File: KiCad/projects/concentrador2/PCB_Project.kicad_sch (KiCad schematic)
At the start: 43 parts, among them J1 54602-908LF, P1 Grabador, P2 Entrada fuente externa, P4 Header 20X2, P5 Header 2, U1 DSPIC33EP256MC202-I/SP, U2 STEP_DOWN_CONVERTER, U3 LD33V, U4 MAX485, U5 DS3234S#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

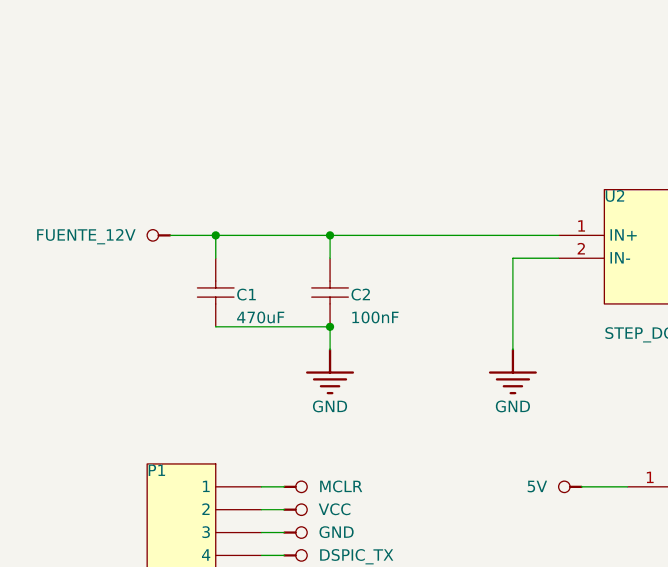
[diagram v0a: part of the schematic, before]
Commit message: Migracion a SMD
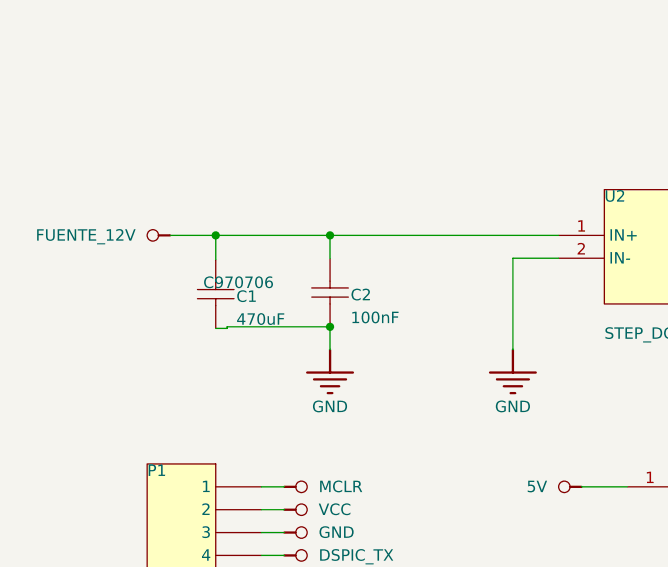
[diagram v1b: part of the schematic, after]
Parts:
- C1: LCSC (none) -> C970706
- R1: footprint F__UDecimo_practicasLaborales2_proyectos_archivosAltium_completos_int3_R-007 ACELEROGRAFO ADXL355 CONCENTRADOR V1_PCB_P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 -> Resistor_SMD:R_0603_1608Metric
- R13, R14, R15, R16, R17, R18, R3, R4: footprint AXIAL-0.3 -> Resistor_SMD:R_0603_1608Metric
- R2, R5: footprint AXIAL-0.3 RES-1/4W -> Resistor_SMD:R_0603_1608Metric
- U3: footprint SOT-223 -> Package_TO_SOT_SMD:SOT-223

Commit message: Fase 3
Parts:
- C10: LCSC (none) -> C3845218
- C12, C13, C15, C2, C4, C5, C7: LCSC (none) -> C141382
- C3: LCSC (none) -> C970695
- C6: LCSC (none) -> C53084506
- Ce: renamed from C8; LCSC (none) -> C141382
- Ce: renamed from C9; LCSC (none) -> C53084506
- R1, R16, R18: LCSC (none) -> C17902
- R13, R14, R2, R5: LCSC (none) -> C22978
- R15, R17: LCSC (none) -> C17903
- R3: LCSC (none) -> C17900
- R4: LCSC (none) -> C17935
- S1: LCSC (none) -> C231329
- U3: LCSC (none) -> C35879
- U4, U9: LCSC (none) -> C481667

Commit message: Fase 4 - Asignación para PCBA
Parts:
- removed BT1: Bateria, Bateria-DS1307, symbol LibreriaRSA:root_0_BateriaDS1307_LibreriaRSA.IntLib
- removed D1: 1N914, DO-35, symbol Miscellaneous Devices:root_0_Diode 1N914_Miscellaneous Devices.IntLib
- added BT2: Battery, Battery:BatteryHolder_Keystone_500, symbol Device:Battery
- added D1: 1N914, Diode_THT:D_DO-35_SOD27_P7.62mm_Horizontal, symbol Diode:1N914
- C1: footprint C100UFB -> Capacitor_SMD:C_Elec_8x10.2; LCSC C970706 -> C2858857
- C10: footprint RAD0.2 -> Capacitor_SMD:C_0402_1005Metric; LCSC C3845218 -> C29266
- C12, C13, C15, C2, C4, C5, C6, C7: footprint RAD0.2 -> Capacitor_SMD:C_0402_1005Metric
- C3: footprint C100UFB -> Capacitor_SMD:C_Elec_6.3x7.7
- C8, C9: renamed from Ce; footprint RAD0.2 -> Capacitor_SMD:C_0402_1005Metric
- D2, D4, D5: footprint F__UDecimo_practicasLaborales2_proyectos_archivosAltium_completos_int3_R-007 ACELEROGRAFO ADXL355 CONCENTRADOR V1_PCB_P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 -> LED_SMD:LED_0603_1608Metric
- GPS1: footprint GPS_BREAKOUT_V3 -> (none)
- J1: footprint *AMPHENOL_54602-908LF -> Connector_RJ:RJ45_Amphenol_54602-x08_Horizontal
- P1: footprint HDR1X6 -> Connector_PinHeader_2.54mm:PinHeader_1x06_P2.54mm_Vertical
- P2: footprint MOLEX-2 -> Connector_JST:JST_XH_B2B-XH-A_1x02_P2.50mm_Vertical
- P4: footprint C__Users_Public_Documents_Altium_AD16_Library_Miscellaneous Connectors_Miscellaneous Connectors_3D.PcbLib:HDR2X20 -> Connector_PinHeader_2.54mm:PinHeader_2x20_P2.54mm_Vertical
- P5: footprint Header 1X2 -> Connector_PinHeader_2.54mm:PinHeader_1x02_P2.54mm_Vertical
- R1, R16, R18: footprint Resistor_SMD:R_0603_1608Metric -> Resistor_SMD:R_1206_3216Metric; LCSC C17902 -> C1469
- R13: value Res1 -> 3K3; footprint Resistor_SMD:R_0603_1608Metric -> Resistor_SMD:R_1206_3216Metric; LCSC C22978 -> C26032
- R14, R2, R5: footprint Resistor_SMD:R_0603_1608Metric -> Resistor_SMD:R_1206_3216Metric; LCSC C22978 -> C26032
- R15: value Res1 -> 10k; footprint Resistor_SMD:R_0603_1608Metric -> Resistor_SMD:R_1206_3216Metric; symbol Miscellaneous Devices:root_1_Res1_Miscellaneous Devices.IntLib -> Device:R_US; LCSC C17903 -> C1489
- R17: footprint Resistor_SMD:R_0603_1608Metric -> Resistor_SMD:R_1206_3216Metric; LCSC C17903 -> C1489
- R3: footprint Resistor_SMD:R_0603_1608Metric -> Resistor_SMD:R_1206_3216Metric; LCSC C17900 -> C17936
- R4: footprint Resistor_SMD:R_0603_1608Metric -> Resistor_SMD:R_1206_3216Metric; LCSC C17935 -> C17900
- S1: footprint PULSA4 -> Button_Switch_SMD:SW_SPST_B3U-1000P
- U1: footprint MCHP-SPDIP-SP28 -> Package_DIP:DIP-28_W7.62mm_LongPads
- U2: footprint STEP_DOWN_CONVERTER -> (none)
- U3: footprint Package_TO_SOT_SMD:SOT-223 -> Package_TO_SOT_SMD:SOT-223-3_TabPin2; symbol LibreriaRSA:root_0_LD33V_LibreriaRSA.IntLib -> Regulator_Linear:LD1117S33TR_SOT223
- U4, U9: footprint DIP794W47P254L991H457Q8 -> Package_SO:SOIC-8_3.9x4.9mm_P1.27mm
- U5: footprint 21-0042B_20 -> Package_SO:SOIC-20W_7.5x12.8mm_P1.27mm
- W1: footprint SIP-2 -> Connector_PinHeader_2.54mm:PinHeader_1x02_P2.54mm_Vertical
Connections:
- net 5V: now also U3.3 (VI); no longer U3.1 (IN)
- net GND: now also U3.1 (GND), BT2.2 (-); no longer U3.2 (GND)
- net VCC: now also U3.2 (VO), D1.2 (A); no longer U3.3 (OUT)
- net at R3.2: now also D1.1 (K)
- net NetBT1_0: now reaches U5.16 (VBAT)
- net NetBT1_0: now also BT2.1 (+)
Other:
- moved on the sheet: U3

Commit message: Fase 4 - 2
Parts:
- C1: value Cap -> 470uF; PACKAGE (none) -> SMD,D8xL10.2mm
- C10: PACKAGE (none) -> 0402
- C12, C13, C15: LCSC C141382 -> C1525; PACKAGE (none) -> 0402
- C2, C4, C5, C7, C8: value Cap -> 100nF; LCSC C141382 -> C1525; PACKAGE (none) -> 0402
- C3: value Cap -> 220uF; PACKAGE (none) -> SMD,D6.3xL7.7mm
- C6, C9: value Cap -> 10nF; LCSC C53084506 -> C15195; PACKAGE (none) -> 0402
- D2, D4, D5: value LED3 -> LED_white; LCSC (none) -> C2290; PACKAGE (none) -> 0603
- R1, R16, R18: LCSC C1469 -> C4410; PACKAGE (none) -> 1206
- R13, R14, R2, R5: footprint Resistor_SMD:R_1206_3216Metric -> Resistor_SMD:R_0805_2012Metric; LCSC C26032 -> C26010; PACKAGE (none) -> 0805
- R15, R17: LCSC C1489 -> C17902; PACKAGE (none) -> 1206
- R3, R4: PACKAGE (none) -> 1206
- S1: LCSC C231329 -> C720477; PACKAGE (none) -> SMD,4x3mm
- U3: PACKAGE (none) -> SOT-223-4SOT-223-4
- U4, U9: PACKAGE (none) -> SOP-8
- U5: LCSC (none) -> C2651511; PACKAGE (none) -> SO-20-300mil

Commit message: Archivos Gerber
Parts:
- BT2, D1, GPS1, J1, P1, P2, P4, P5, U1, U2, W1: now left out of the parts list
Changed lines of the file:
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@@
 		(body_style 1)
 		(exclude_from_sim no)
-		(in_bom yes)
+		(in_bom no)
 		(on_board yes)
-		(in_pos_files yes)
+		(in_pos_files no)
 		(dnp no)
 		(fields_autoplaced yes)
@@
 		(body_style 1)
 		(exclude_from_sim no)
-		(in_bom yes)
+		(in_bom no)
 		(on_board yes)
-		(in_pos_files yes)
+		(in_pos_files no)
 		(dnp no)
 		(property "Reference" "U1"
@@
 		(body_style 1)
 		(exclude_from_sim no)
-		(in_bom yes)
+		(in_bom no)
 		(on_board yes)
-		(in_pos_files yes)
+		(in_pos_files no)
 		(dnp no)
 		(property "Reference" "P1"
@@
 		(body_style 1)
 		(exclude_from_sim no)
-		(in_bom yes)
+		(in_bom no)
 		(on_board yes)
-		(in_pos_files yes)
+		(in_pos_files no)
 		(dnp no)
 		(property "Reference" "P2"
@@
 		(body_style 1)
 		(exclude_from_sim no)
-		(in_bom yes)
+		(in_bom no)
 		(on_board yes)
-		(in_pos_files yes)
+		(in_pos_files no)
 		(dnp no)
 		(property "Reference" "GPS1"
@@
 		(body_style 1)
 		(exclude_from_sim no)
-		(in_bom yes)
+		(in_bom no)
 		(on_board yes)
-		(in_pos_files yes)
+		(in_pos_files no)
 		(dnp no)
 		(property "Reference" "W1"
@@
 		(body_style 1)
 		(exclude_from_sim no)
-		(in_bom yes)
+		(in_bom no)
 		(on_board yes)
-		(in_pos_files yes)
+		(in_pos_files no)
 		(dnp no)
 		(property "Reference" "U2"
@@
 		(body_style 1)
 		(exclude_from_sim no)
-		(in_bom yes)
+		(in_bom no)
 		(on_board yes)
-		(in_pos_files yes)
+		(in_pos_files no)
 		(dnp no)
 		(property "Reference" "J1"
@@
 		(body_style 1)
 		(exclude_from_sim no)
-		(in_bom yes)
+		(in_bom no)
 		(on_board yes)
-		(in_pos_files yes)
+		(in_pos_files no)
 		(dnp no)
 		(property "Reference" "P5"
@@
 		(body_style 1)
 		(exclude_from_sim no)
-		(in_bom yes)
+		(in_bom no)
 		(on_board yes)
-		(in_pos_files yes)
+		(in_pos_files no)
 		(dnp no)
 		(fields_autoplaced yes)
@@
 		(body_style 1)
 		(exclude_from_sim no)
-		(in_bom yes)
+		(in_bom no)
 		(on_board yes)
-		(in_pos_files yes)
+		(in_pos_files no)
 		(dnp no)
 		(property "Reference" "P4"
